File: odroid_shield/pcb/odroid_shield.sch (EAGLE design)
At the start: 69 parts, among them J1 AVRISP6_COMPACT, J4 ODROID_J4, U1 SINGLE-BIT_BUS_TRANSCEIVER, U10 ABM8G, U2 SINGLE-BIT_BUS_TRANSCEIVER, U3 ST1S10, U4 ATMEGA644P-20AU, U5 TS5205, U6 TCA9517MSOP8, U7 MP33926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

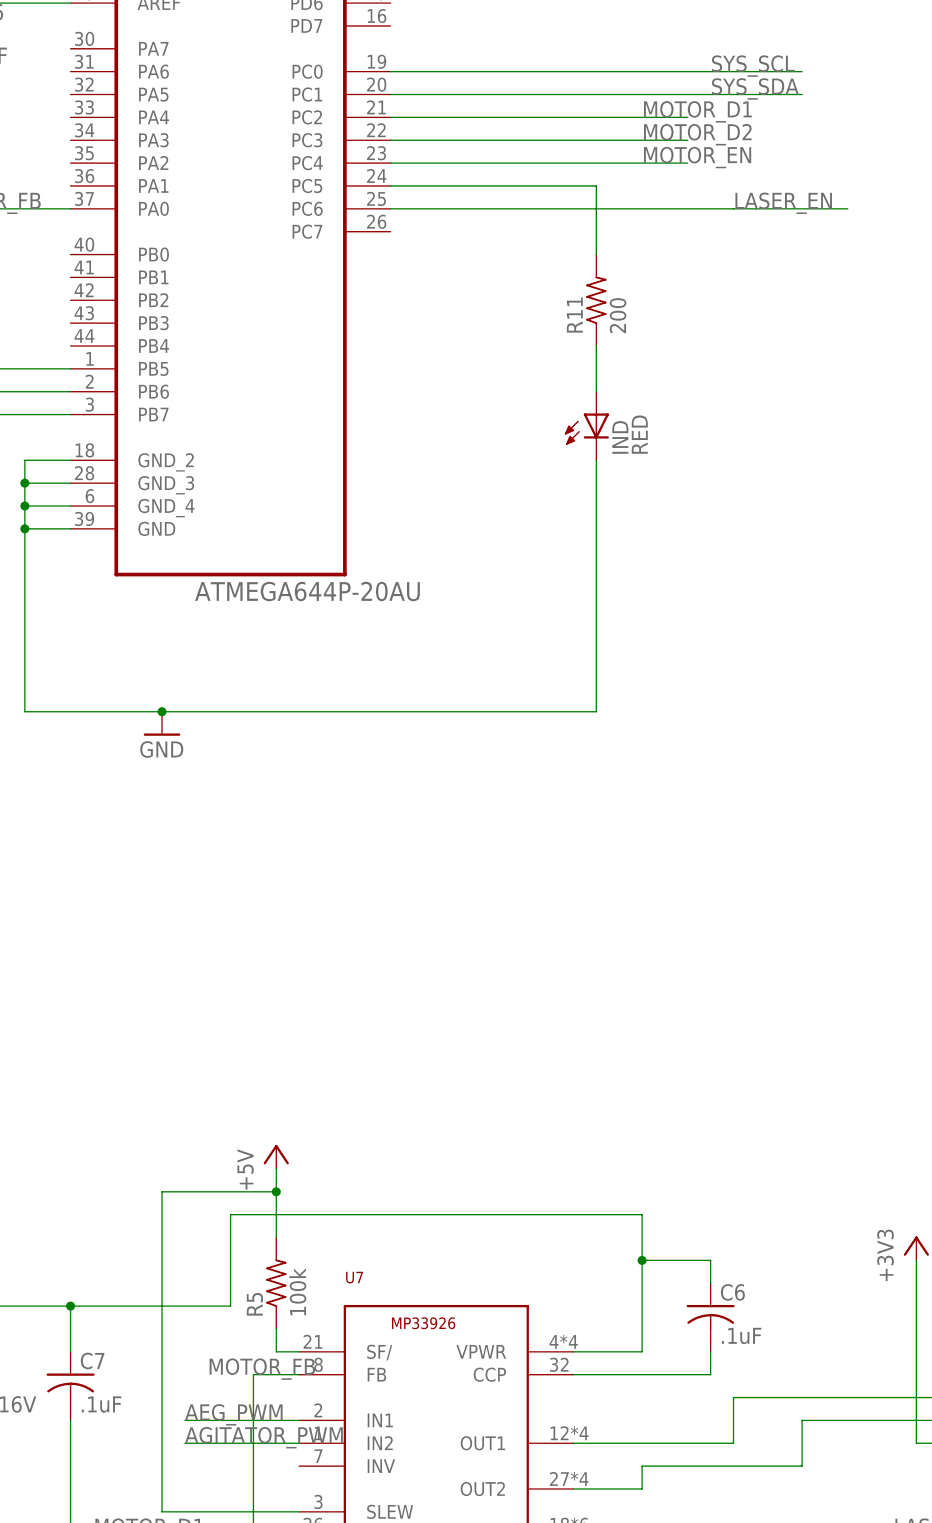
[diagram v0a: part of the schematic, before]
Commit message: odroid_shield: Connect up the 33926's status pin to the AVR.
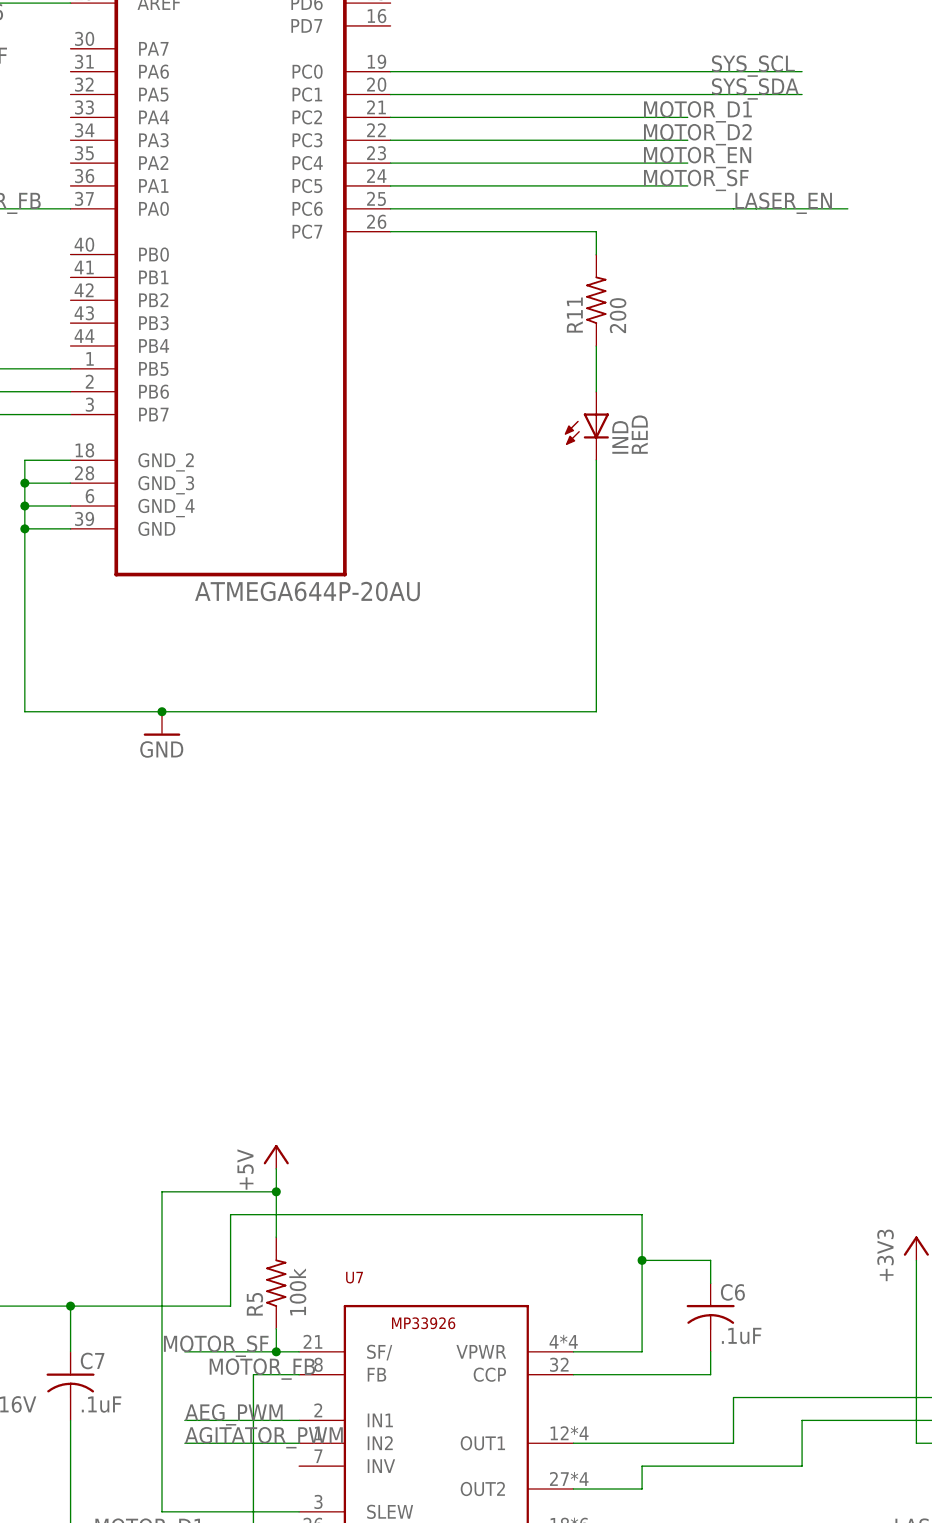
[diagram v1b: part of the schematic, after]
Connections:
- removed net N$29: R11.2, U4.PC5
- new net MOTOR_SF: R5.1, U4.PC5, U7.SF/
- net N$17: now also R11.2, U4.PC7; no longer R5.1, U7.SF/
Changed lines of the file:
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@@
 </segment>
 </net>
-<net name="N$17" class="0">
+<net name="MOTOR_SF" class="0">
 <segment>
 <pinref part="R5" gate="G$1" pin="1"/>
@@
 <pinref part="U7" gate="G$1" pin="SF/"/>
 <wire x1="91.44" y1="160.02" x2="93.98" y2="160.02" width="0.1524" layer="91"/>
+<wire x1="91.44" y1="160.02" x2="81.28" y2="160.02" width="0.1524" layer="91"/>
+<junction x="91.44" y="160.02"/>
+<label x="78.74" y="160.02" size="1.778" layer="95"/>
+</segment>
+<segment>
+<pinref part="U4" gate="A" pin="PC5"/>
+<wire x1="104.14" y1="289.56" x2="137.16" y2="289.56" width="0.1524" layer="91"/>
+<label x="132.08" y="289.56" size="1.778" layer="95"/>
 </segment>
 </net>
@@
 </segment>
 </net>
-<net name="N$29" class="0">
-<segment>
-<pinref part="R11" gate="G$1" pin="2"/>
-<wire x1="127" y1="281.94" x2="127" y2="289.56" width="0.1524" layer="91"/>
-<pinref part="U4" gate="A" pin="PC5"/>
-<wire x1="127" y1="289.56" x2="104.14" y2="289.56" width="0.1524" layer="91"/>
-</segment>
-</net>
 <net name="N$32" class="0">
 <segment>
@@
 </segment>
 </net>
+<net name="N$17" class="0">
+<segment>
+<pinref part="R11" gate="G$1" pin="2"/>
+<wire x1="127" y1="281.94" x2="127" y2="284.48" width="0.1524" layer="91"/>
+<pinref part="U4" gate="A" pin="PC7"/>
+<wire x1="127" y1="284.48" x2="104.14" y2="284.48" width="0.1524" layer="91"/>
+</segment>
+</net>
